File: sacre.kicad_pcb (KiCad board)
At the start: 4 copper layers, 91.4 x 88.4 mm, 92 parts, among them J1 Touch, J2 Screen, J3 USB_C_Receptacle_USB2.0_16P, J5 +BATT, J6 -BATT, M1 Vibration_Motor, Q1 CJ2312, Q2 S8050, Q3 CJ3415, Q4 SI1308EDL, Q5 CJ3415, Q6 CJ2312, Q7 UMH3N, SW1 TSC02-TDW1FH3.5, U1 LIS3DH, U2 ESP32-PICO-D4, U3 CP2104, U5 TP4054, U6 TLV62568DBVR, Y1 RV-8803-C7-TA-QC

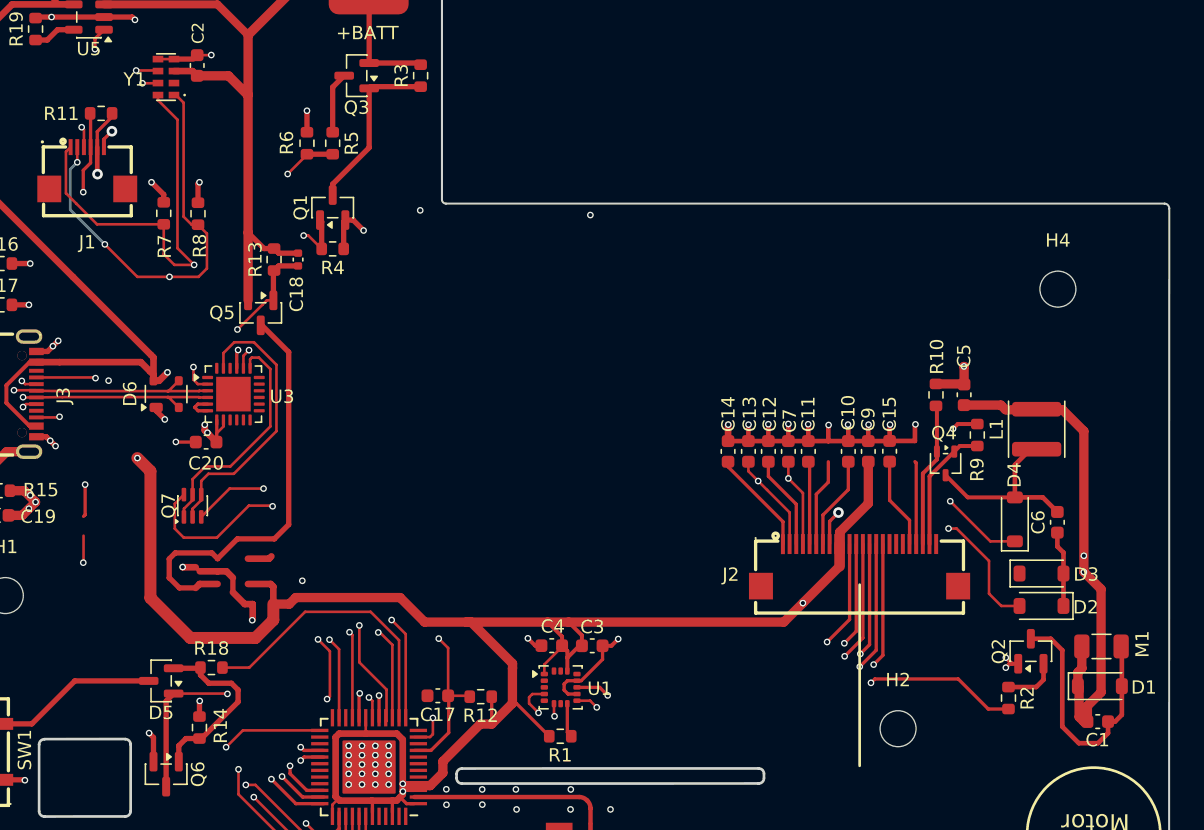
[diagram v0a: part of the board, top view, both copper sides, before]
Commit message: Retira cobre obsoleto y ramas sin destino tras sincronizacion
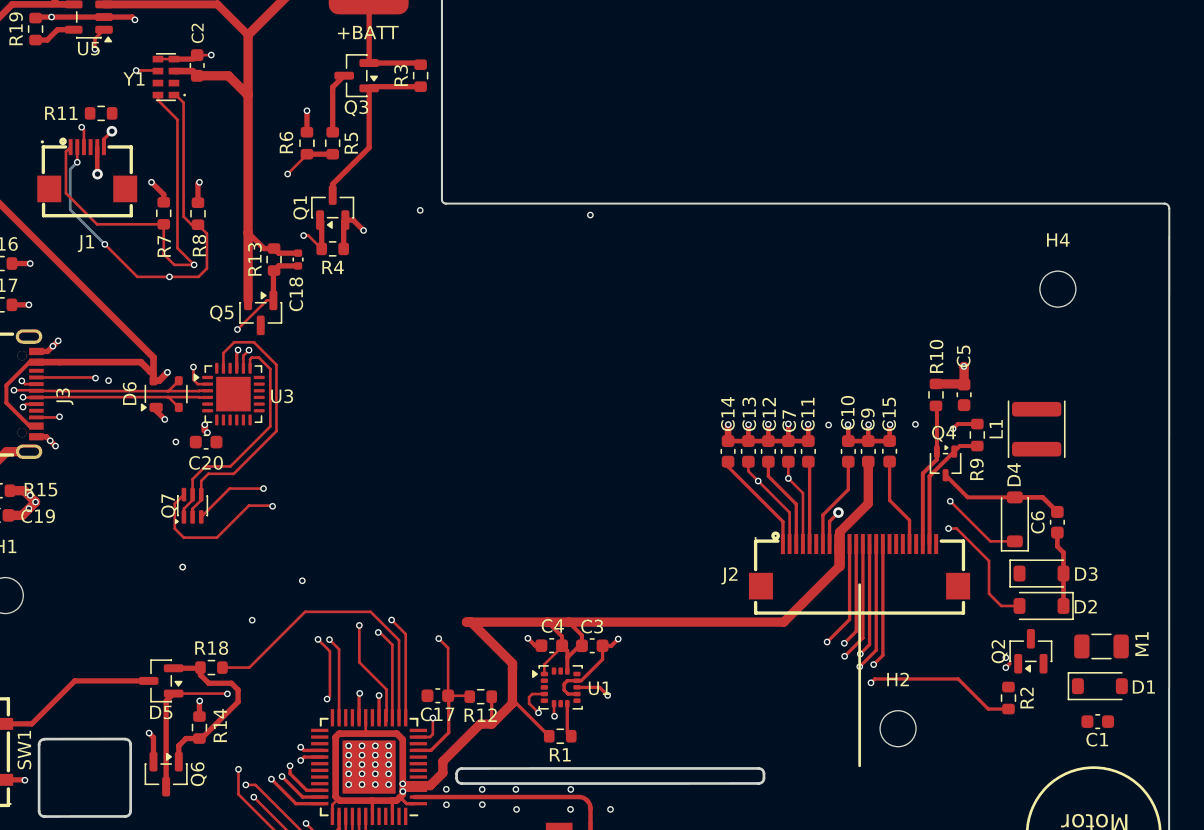
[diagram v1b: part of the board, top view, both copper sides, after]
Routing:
- net +3V3: track 249.0 -> 122.7 mm, vias 10 -> 5
- net RTC_EVI: track 57.7 -> 0.00 mm, vias 2 -> 0
- net Net-(J1-Pin_4): track 32.9 -> 0.00 mm, vias 2 -> 0
- net VSYS: track 31.8 -> 0.09 mm
- net unconnected-(U2-IO16-Pad25): track 28.4 -> 0.00 mm, vias 2 -> 0
- net ACC_INT2: track 21.0 -> 0.00 mm, vias 2 -> 0
- net Net-(D1-A): track 20.0 -> 0.00 mm
- net GND: track 106.3 -> 91.2 mm, vias 80 -> 83
- net unconnected-(J2-Pin_6-Pad6): track 6.55 -> 0.00 mm
- net unconnected-(J2-Pin_21-Pad21): track 6.22 -> 0.00 mm
- net Net-(Q2-B): track 5.76 -> 0.00 mm, vias 2 -> 0
- net USB_VBUS: track 74.2 -> 69.4 mm
- net Net-(D4-A): track 14.1 -> 9.53 mm
- net Net-(U4-SW): track 1.83 -> 0.00 mm

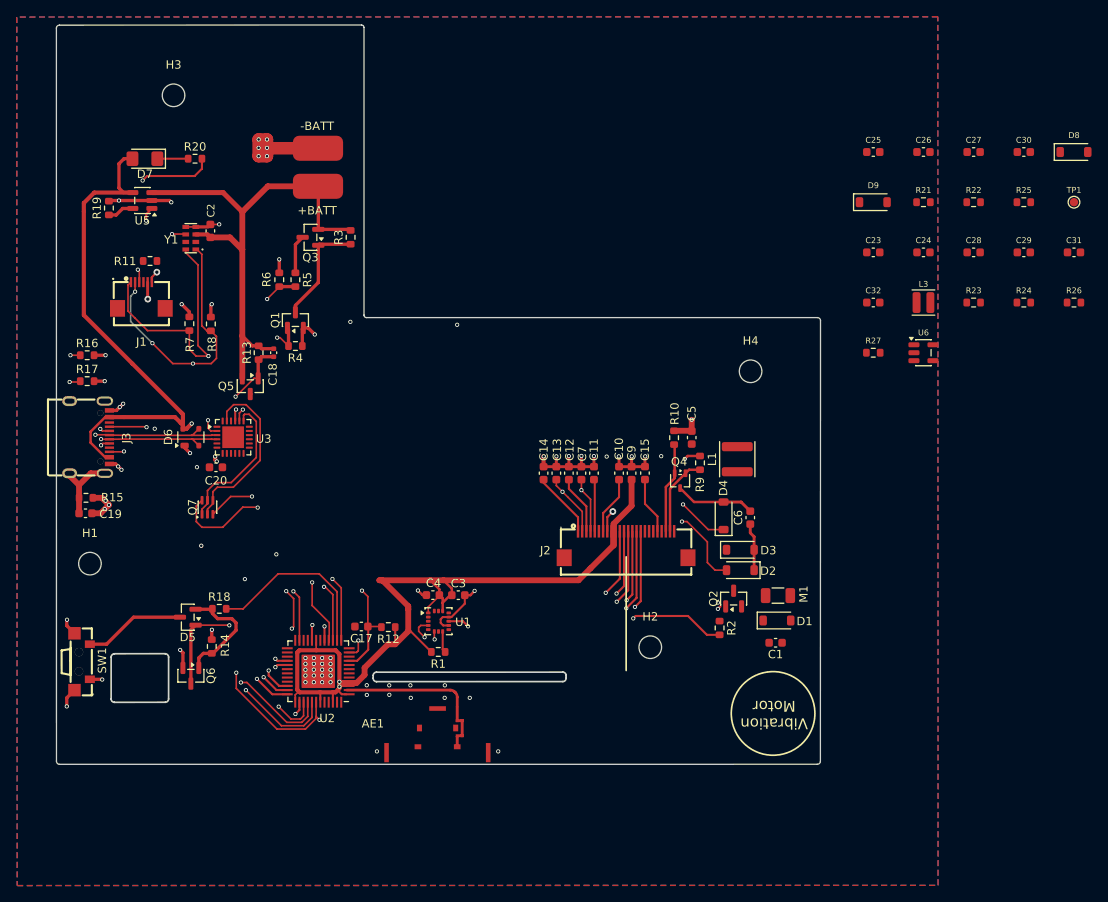
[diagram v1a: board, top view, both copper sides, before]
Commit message: Coloca componentes por zonas y deja PCB preparada para enrutar
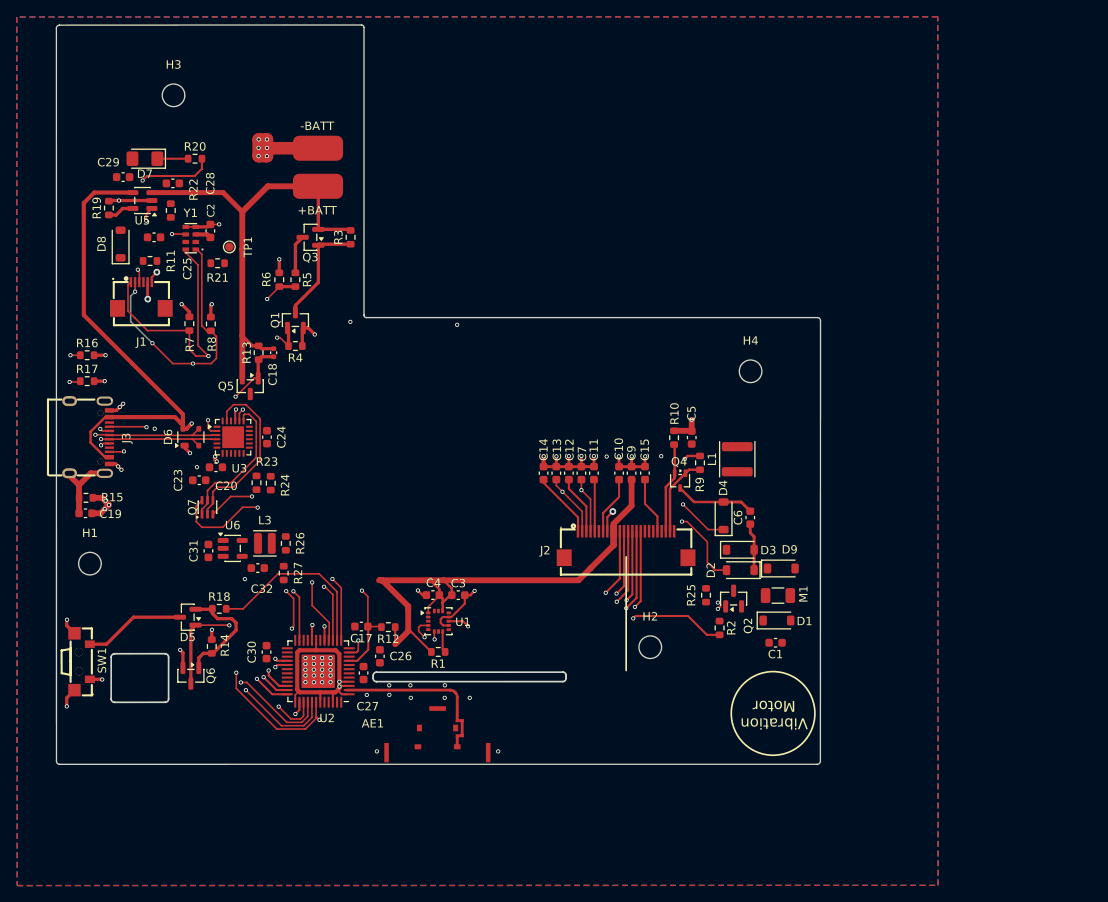
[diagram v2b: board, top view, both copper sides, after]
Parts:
- moved D8 114.5 mm to (57.0, 96.0), turned to 90 degrees
- moved C31 109.5 mm to (67.5, 132.7), turned to 90 degrees
- moved C30 108.5 mm to (74.5, 144.8), turned to 90 degrees
- moved C29 108.1 mm to (57.3, 88.0)
- moved TP1 101.1 mm to (70.0, 96.3)
- moved R26 98.6 mm to (76.8, 131.8), turned to 90 degrees
- moved C28 96.1 mm to (63.2, 88.8)
- moved R22 96.0 mm to (63.0, 92.0), turned to 90 degrees
- moved C27 95.9 mm to (86.0, 147.3), turned to 90 degrees
- moved R24 92.6 mm to (75.0, 124.6), turned to 90 degrees
- moved C26 88.7 mm to (88.0, 145.3), turned to 90 degrees
- moved R23 88.4 mm to (73.2, 124.5), turned to 90 degrees
- moved C25 86.6 mm to (61.0, 95.2)
- moved U6 85.9 mm to (70.4, 132.4)
- moved C23 85.1 mm to (66.4, 124.2)
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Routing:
- net +3V3: track 122.7 -> 113.7 mm
- net USB_VBUS: track 69.4 -> 62.7 mm
- net VBAT_RAW: track 61.8 -> 57.3 mm
- net GND: track 91.2 -> 88.8 mm, vias 83 -> 79

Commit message: Guarda PCB enrutada y revisada con reglas JLCPCB y correccion de J3
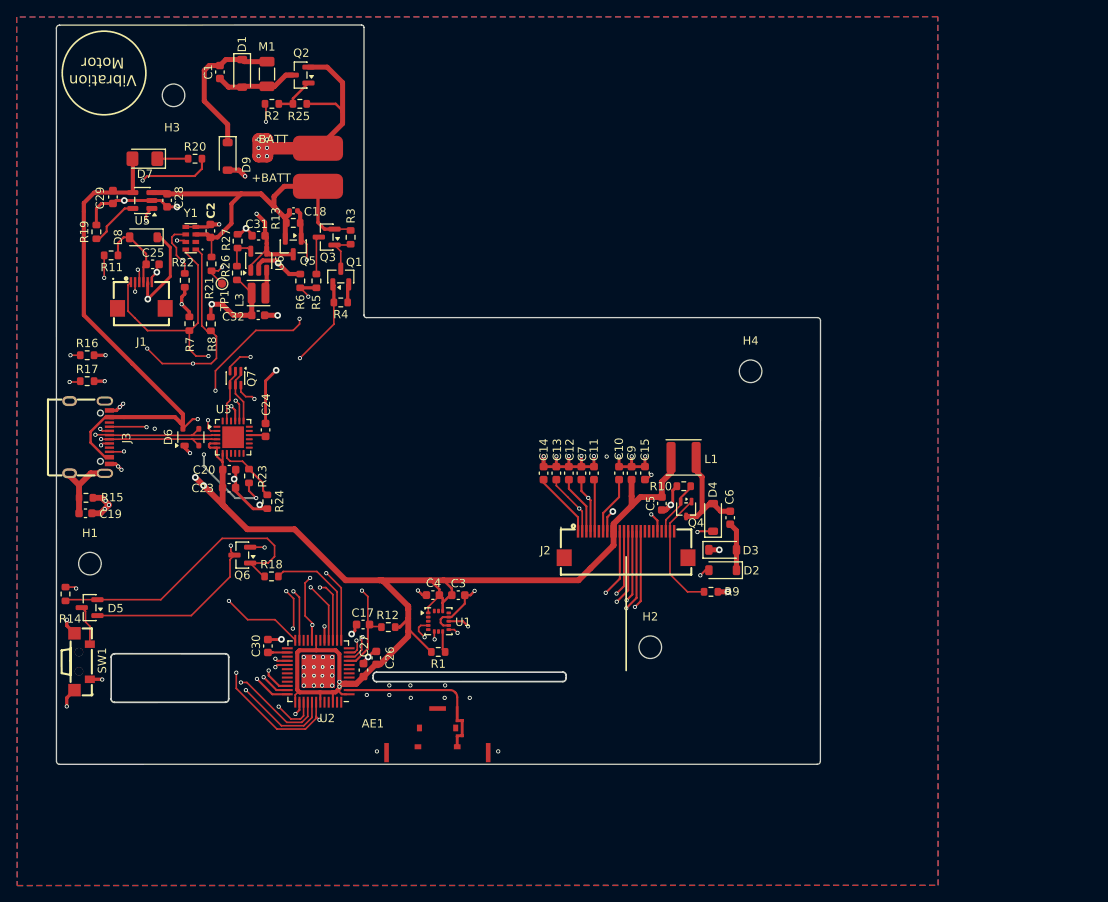
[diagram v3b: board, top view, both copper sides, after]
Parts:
- moved C1 95.3 mm to (68.9, 75.4), turned to -90 degrees
- moved D1 91.5 mm to (71.5, 75.6), turned to -90 degrees
- moved M1 87.3 mm to (74.5, 75.7), turned to -90 degrees
- moved D9 82.5 mm to (69.8, 85.5), turned to -90 degrees
- moved R2 82.4 mm to (75.1, 79.2), turned to 180 degrees
- moved Q2 81.2 mm to (78.5, 75.8), turned to 180 degrees
- moved R25 76.2 mm to (78.4, 79.2), turned to 0 degrees
- moved R27 40.1 mm to (71.0, 95.7)
- moved C31 38.2 mm to (73.5, 95.0), turned to 180 degrees
- moved U6 34.5 mm to (73.5, 98.0), turned to 90 degrees
- moved R26 32.9 mm to (70.9, 99.5), turned to -90 degrees
- moved C32 30.2 mm to (73.5, 104.5)
- moved L3 29.9 mm to (73.5, 101.9), turned to 180 degrees
- moved R14 18.6 mm to (50.4, 137.8)
- moved Q5 17.5 mm to (77.6, 96.3)
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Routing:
- net +3V3: track 113.7 -> 209.2 mm, vias 5 -> 7
- net RES_TOUCH_CTRL: track 0.00 -> 57.4 mm, vias 0 -> 2
- net GND: track 88.8 -> 143.7 mm, vias 79 -> 77
- net Net-(Q6-G): track 13.8 -> 35.4 mm
- net Vibration_PWM: track 52.2 -> 71.3 mm, vias 2 -> 3
- net VSYS: track 0.09 -> 18.9 mm, vias 0 -> 2
- net /VMOTOR: track 0.00 -> 17.9 mm
- net Net-(Q5-G): track 52.9 -> 70.3 mm, vias 2 -> 4
- net ACC_INT2: track 0.00 -> 16.7 mm, vias 0 -> 2
- net DTR: track 21.3 -> 6.38 mm
- net GPIO0: track 25.4 -> 40.1 mm
- net USB_VBUS: track 62.7 -> 77.0 mm
- net RTC_EVI: track 0.00 -> 11.3 mm, vias 0 -> 2
- net RTS: track 17.5 -> 6.63 mm
- net Net-(D1-A): track 0.00 -> 9.74 mm
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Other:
- outline, holes or cut-outs redrawn

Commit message: Cierra revision PCB y prepara pedido JLCPCB
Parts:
- added R28: 1k, Resistor_SMD:R_0603_1608Metric, F.Cu at (55.8, 98.9)
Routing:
- net Net-(D8-A): track 9.47 -> 11.1 mm
- net RES_TOUCH_CTRL: track 57.4 -> 58.5 mm
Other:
- board text added: "RF /ANT_RF hacia AE1: calculada con JLCPCB, 50,15 ohm nominales. Apilado JLC04101H-7628; calculo con mascara incluida. Recalcular si cambia apilado, mascara o geometria. Parametros y limites: README, seccion Pista RF."
